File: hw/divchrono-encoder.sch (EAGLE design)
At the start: 0 parts

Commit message: Laid out major board connections/pin mappings, and started on framework for encoder and amplifier boards. Minor documentation updates to reflect changes.
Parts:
- added C1, C4: 100nF, rcl:C-USC1206
- added C2, C3: 22pF, rcl:C-USC1206
- added J1: (no value), pinhead:PINHD-2X3
- added J2: (no value), pinhead:PINHD-1X6
- added U1: PIC16F54-I/P, Microchip_By_element14_Batch_1:PIC16F54-I/P
- added X1: 32KHz, pgrmcount:CRYSTALS-NOGND-WATCH-3X8
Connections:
- new net +3V3: C1.1, C4.1, J1.2, J2.2, U1.VDD
- new net 1: U1.RA0
- new net 2: U1.RA1
- new net 3: U1.RA2
- new net 4: U1.RA3
- new net 5: U1.RB3
- new net 6: U1.RB4
- new net 7: U1.RB5
- new net D1: J1.1, U1.RB0
- new net D2: J1.3, U1.RB1
- new net D3: J1.5, U1.RB2
- new net GND: C1.2, C2.2, C3.2, C4.2, J1.6, J2.3, U1.VSS
- new net OSC1: C2.1, U1.OSC1/CLKIN, X1.1
- new net OSC2: C3.1, U1.OSC2/CLKOUT, X1.2
- new net PGC: J2.5, U1.RB6/ICSPCLK
- new net PGD: J2.4, U1.RB7/ICSPDAT
- new net VPP: J2.1, U1.~MCLR/VPP

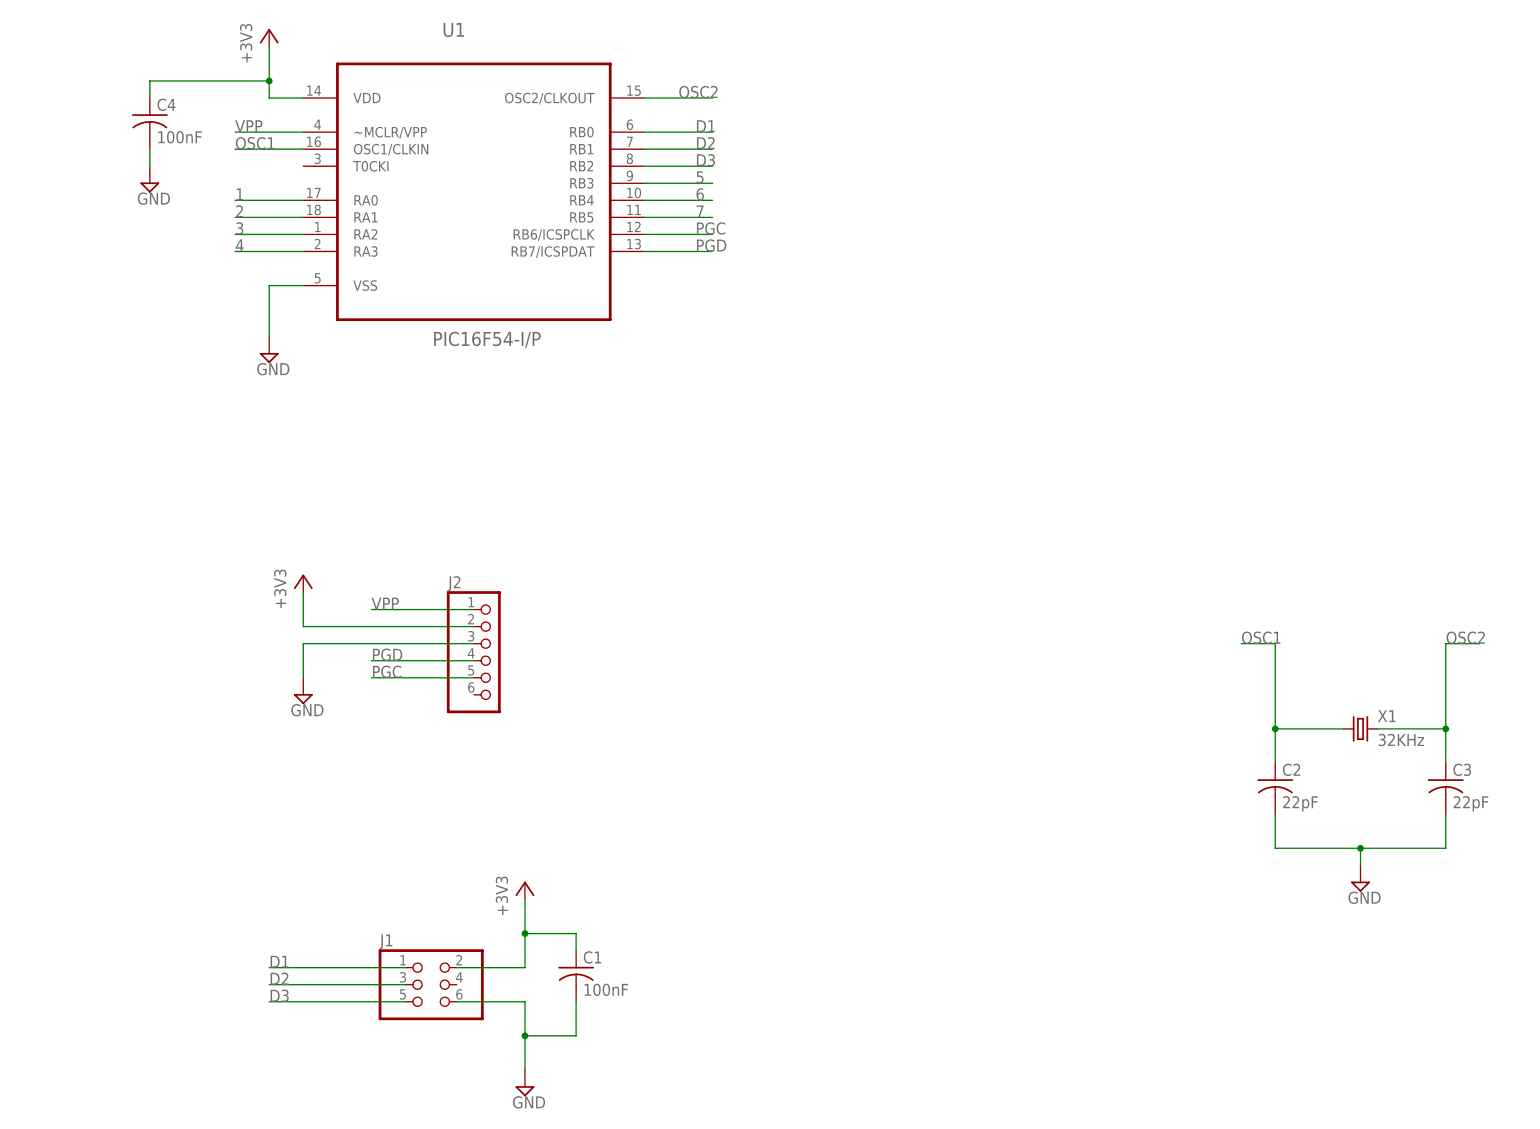
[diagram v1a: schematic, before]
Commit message: Updated encoder board and documentation for new design using a SN74HC148 encoder instead of a custom PIC.
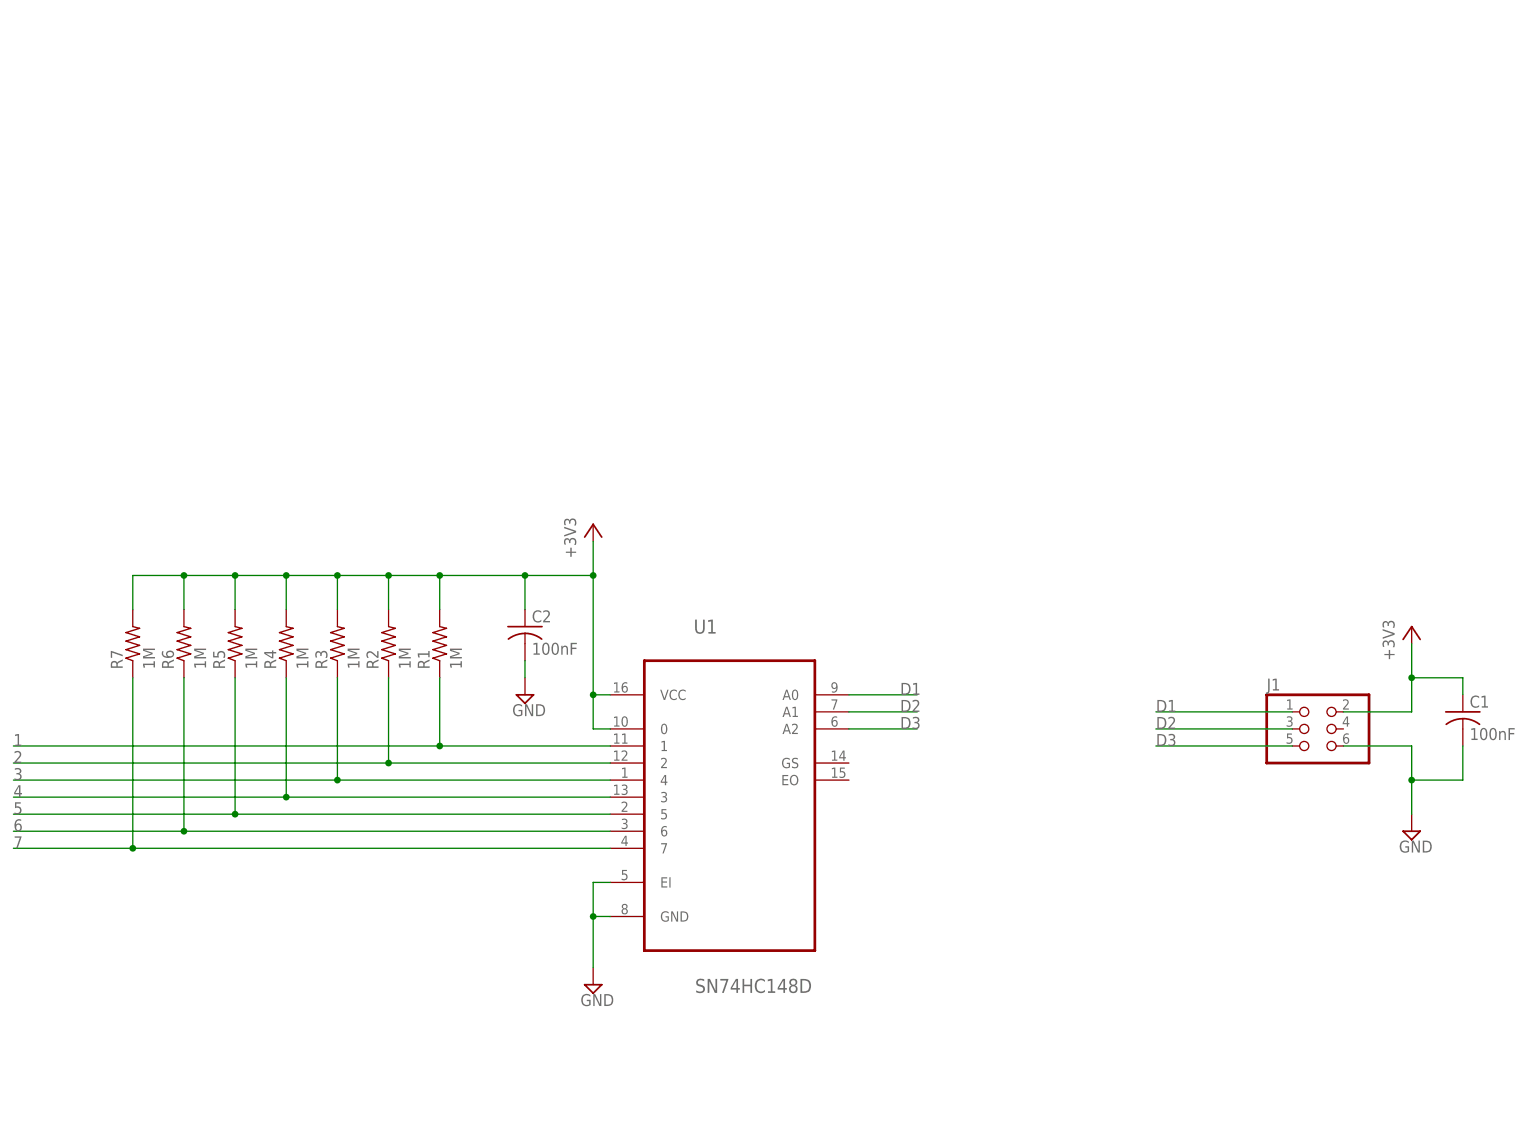
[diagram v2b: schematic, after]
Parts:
- removed C3: 22pF, rcl:C-USC1206
- removed C4: 100nF, rcl:C-USC1206
- removed J2: (no value), pinhead:PINHD-1X6
- removed X1: 32KHz, pgrmcount:CRYSTALS-NOGND-WATCH-3X8
- added R1, R2, R3, R4, R5, R6, R7: 1M, rcl:R-US_M1206
- C2: value 22pF -> 100nF
- U1: value PIC16F54-I/P -> SN74HC148D; device Microchip_By_element14_Batch_1:PIC16F54-I/P -> Texas Instruments_By_element14_Batch_1:SN74HC148D
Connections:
- removed net OSC1: C2.1, U1.OSC1/CLKIN, X1.1
- removed net OSC2: C3.1, U1.OSC2/CLKOUT, X1.2
- removed net PGC: J2.5, U1.RB6/ICSPCLK
- removed net PGD: J2.4, U1.RB7/ICSPDAT
- removed net VPP: J2.1, U1.~MCLR/VPP
- net +3V3: now also C2.1, R1.2, R2.2, R3.2, R4.2, R5.2, R6.2, R7.2, U1.0, U1.VCC; no longer C4.1, J2.2, U1.VDD
- net 1: now also R1.1, U1.1; no longer U1.RA0
- net 2: now also R2.1, U1.2; no longer U1.RA1
- net 3: now also R3.1, U1.4; no longer U1.RA2
- net 4: now also R4.1, U1.3; no longer U1.RA3
- net 5: now also R5.1, U1.5; no longer U1.RB3
- net 6: now also R6.1, U1.6; no longer U1.RB4
- net 7: now also R7.1, U1.7; no longer U1.RB5
- net D1: now also U1.A0; no longer U1.RB0
- net D2: now also U1.A1; no longer U1.RB1
- net D3: now also U1.A2; no longer U1.RB2
- net GND: now also U1.EI, U1.GND; no longer C3.2, C4.2, J2.3, U1.VSS
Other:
- moved on the sheet: C1, C2, J1

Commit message: Finished initial encoder board schematic and layout. Checked ERC/DRC, updated documentation, and compiled gerbers.
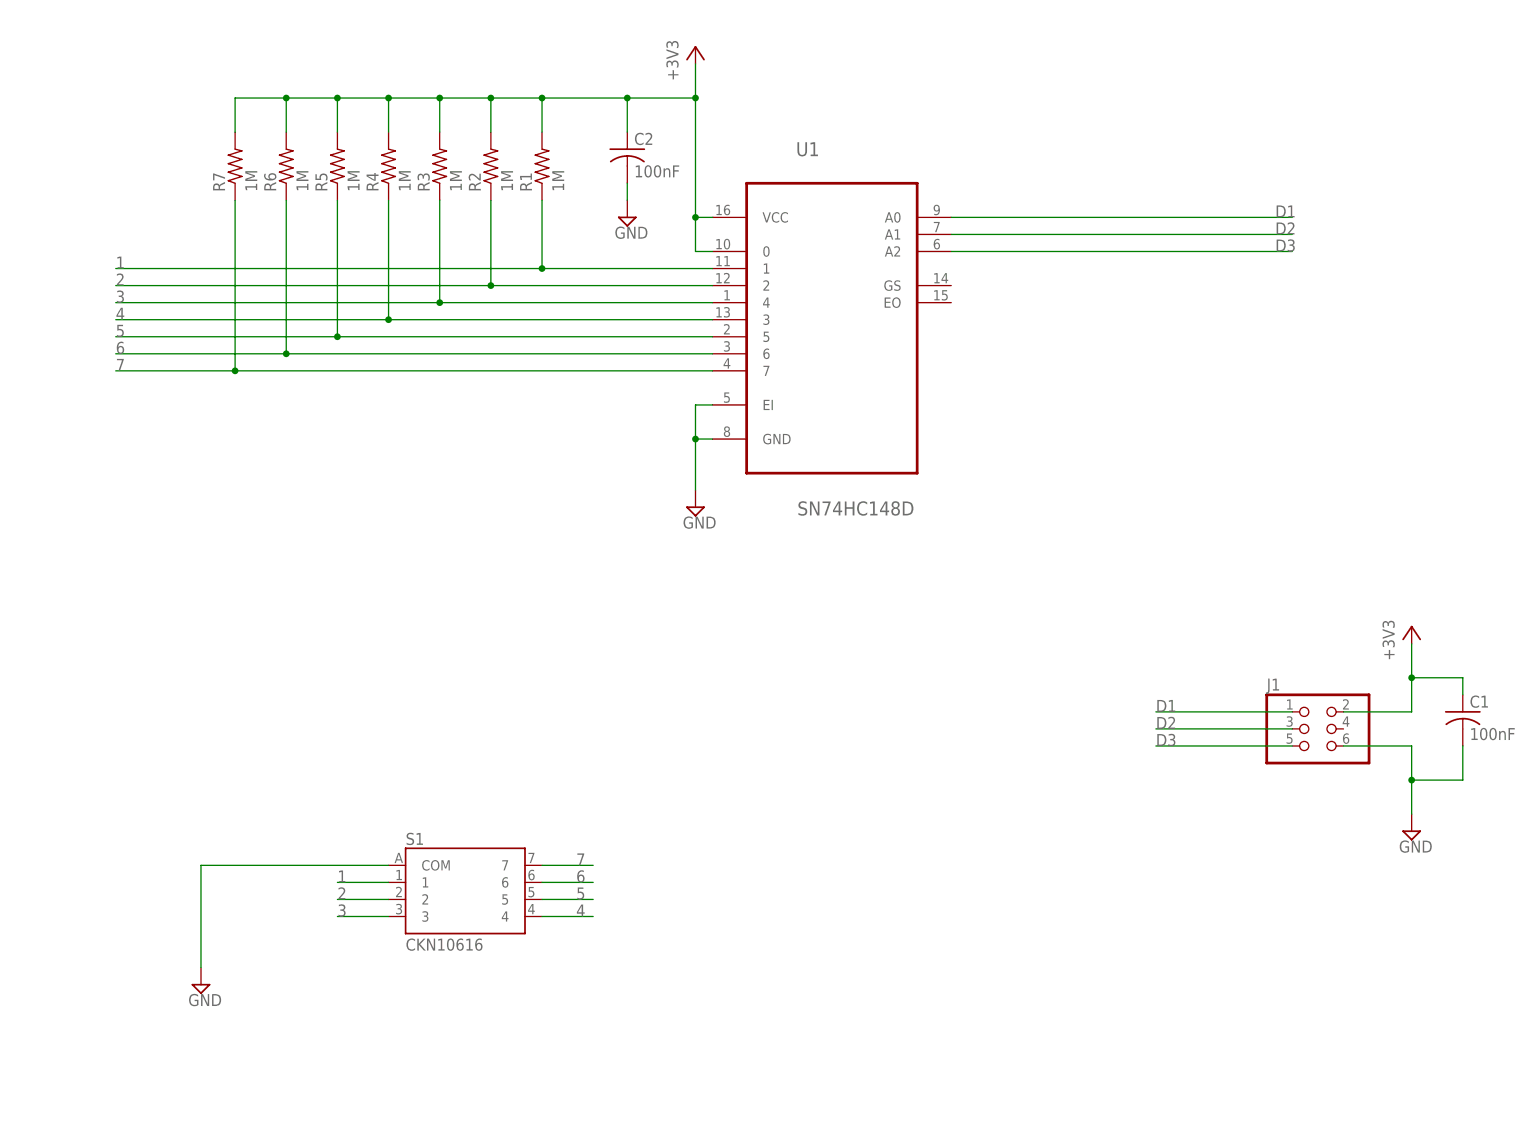
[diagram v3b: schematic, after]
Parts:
- added S1: CKN10616, divchrono:CKN10616
- R1, R2, R3, R4, R5, R6, R7: device rcl:R-US_M1206 -> rcl:R-US_R1206
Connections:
- net 1: now also S1.1
- net 2: now also S1.2
- net 3: now also S1.3
- net 4: now also S1.4
- net 5: now also S1.5
- net 6: now also S1.6
- net 7: now also S1.7
- net GND: now also S1.COM
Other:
- moved on the sheet: C2, R1, R2, R3, R4, R5, R6, R7, U1
